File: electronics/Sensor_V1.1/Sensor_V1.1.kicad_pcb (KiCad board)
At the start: 2 copper layers, 45.9 x 25.6 mm, 44 parts, among them J1 nuclone_small_left, J2 nuclone_small_right, J5 DevBoardUartInput, Q1 DMG1012, Q2 DMG1012, Q3 DMG1012, U1 PPG_sensor, U2 reference_sot23-3, U3 MCP6541

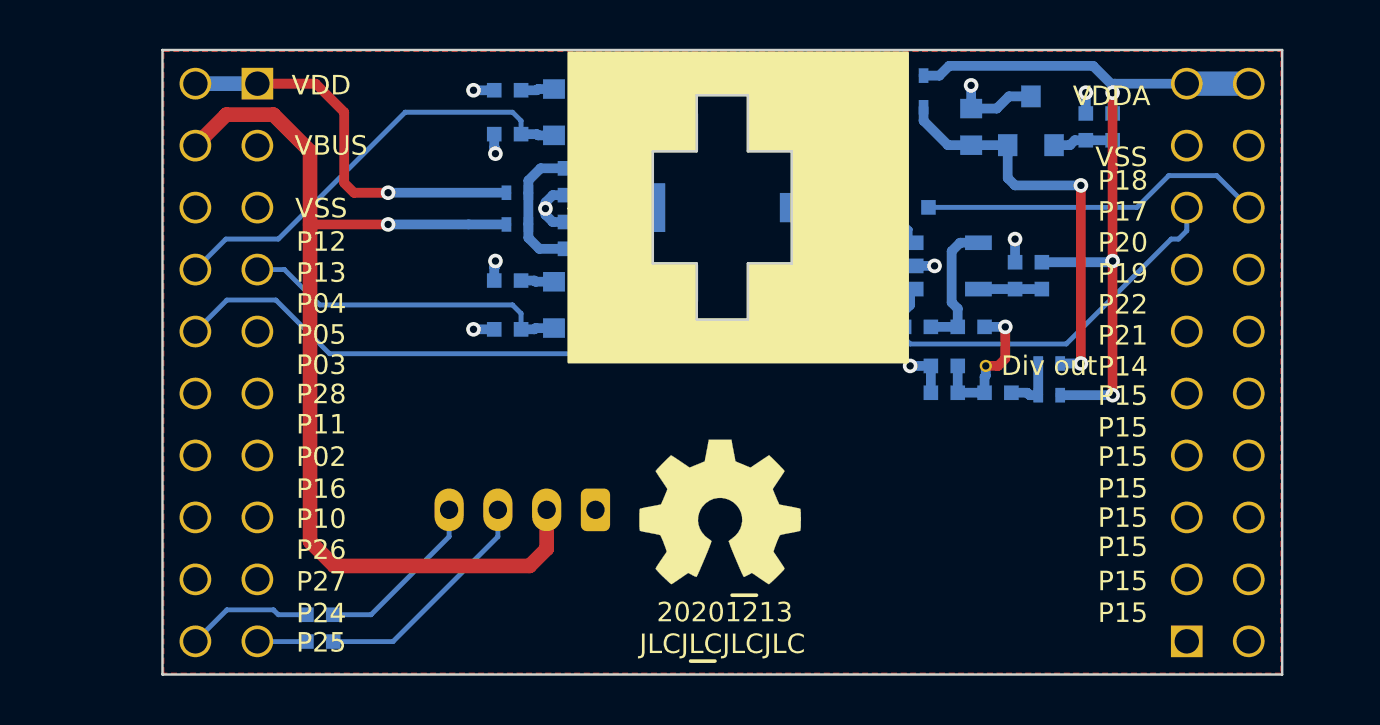
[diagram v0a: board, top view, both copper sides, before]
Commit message: wrong header placement
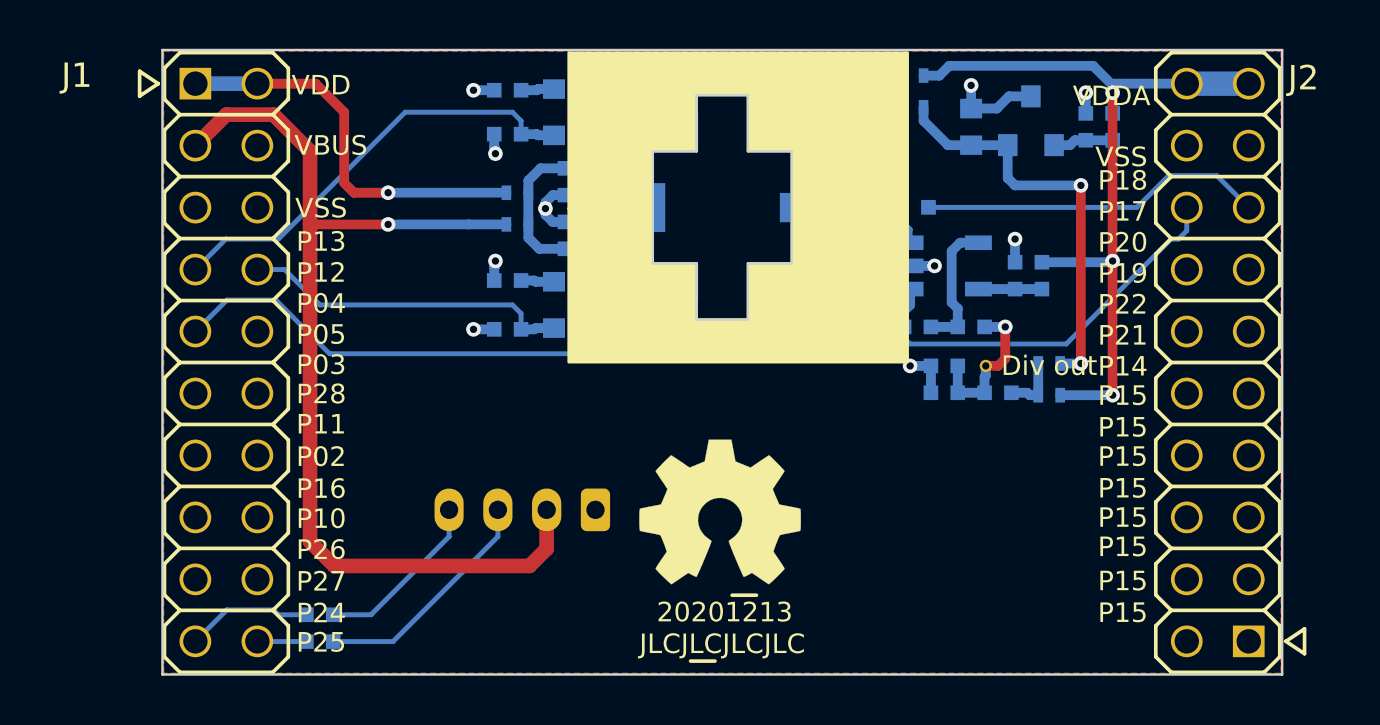
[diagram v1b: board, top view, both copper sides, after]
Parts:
- J1, J2: moved to F.Cu

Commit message: renaming labels, fixxing some routing
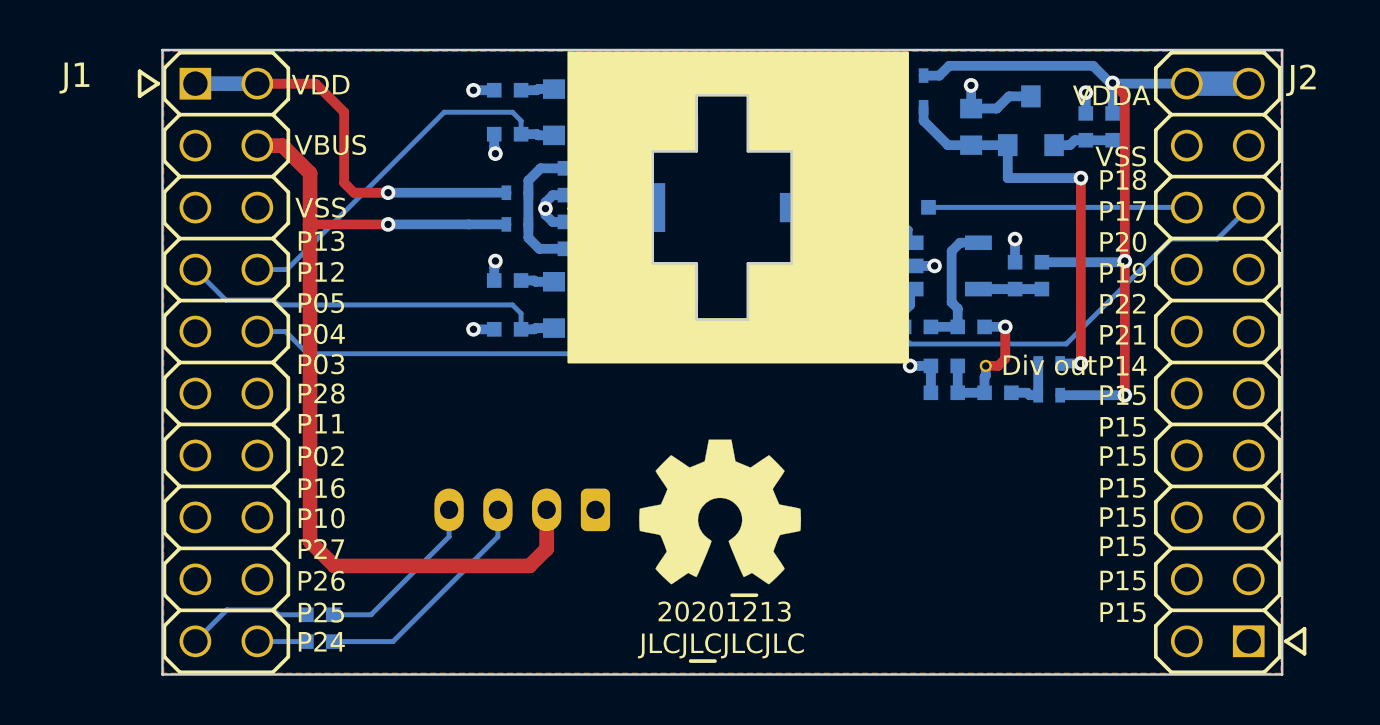
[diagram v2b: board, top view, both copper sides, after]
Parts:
- C9: footprint SquantorRcl:C_0805 -> SquantorRcl:C_0805+0603
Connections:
- J1 pad 19: /UART_TX -> /UART_RX
- J1 pad 20: /UART_RX -> /UART_TX
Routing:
- net /VBUS: track 41.9 -> 37.8 mm
- net /PD_ADC: track 14.2 -> 10.6 mm
- net /I_reset: track 31.3 -> 27.7 mm
- net /LED2_EN: track 18.1 -> 15.5 mm
- net /LED1_EN: track 13.6 -> 16.1 mm
- net /CMP_OUT: track 16.7 -> 18.7 mm
- net /VDDA: track 32.5 -> 34.3 mm
